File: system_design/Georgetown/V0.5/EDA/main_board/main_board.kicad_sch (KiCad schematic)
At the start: 32 parts, among them J1 B3B-XH-A_LF__SN_, J2 Conn_01x02_Pin, P1 SD card socket, SW1 SW_Wuerth_450301014042, U1 HX-2S-JH10, U2 DS3231M, U3 INA219AxD, U4 BME280_module, U5 KA78M05_TO252

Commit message: PCB updated - cosmetics
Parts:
- C1, C2, C4: value C -> 0.1uF
- C3: value C -> 22uF
- R2: value Rs -> 0.1
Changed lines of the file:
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@@
 			)
 		)
-		(property "Value" "C"
+		(property "Value" "0.1uF"
 			(at 241.3 147.5994 90)
 			(effects
@@
 			)
 		)
-		(property "Value" "Rs"
+		(property "Value" "0.1"
 			(at 98.298 43.053 0)
 			(effects
@@
 			)
 		)
-		(property "Value" "C"
+		(property "Value" "0.1uF"
 			(at 108.331 43.053 0)
 			(effects
@@
 			)
 		)
-		(property "Value" "C"
+		(property "Value" "0.1uF"
 			(at 104.521 57.023 0)
 			(effects
@@
 			)
 		)
-		(property "Value" "C"
+		(property "Value" "22uF"
 			(at 74.041 57.023 0)
 			(effects

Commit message: PCB correction for v0.5
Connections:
- net 3V3: now reaches A1.17 (3V3), C1.1, C5.1, C6.1, P1.4 (VDD), R3.1, R4.1, R5.2, U2.2 (VCC), U3.5 (VS), U4.1 (VIN), nRF24L01+1.1 (3.3V)
- net nRF_CE: now reaches A1.9 (D6)
- net nRF_CE: now also nRF24L01+1.6 (CE); no longer nRF24L01+1.2 (CSN)
- net MOSI: now reaches A1.14 (D11), R9.1, nRF24L01+1.3 (MOSI)
- net MOSI: no longer R11.1
- net at nRF24L01+1.4 (IRQ): no longer A1.6 (D3)
- net nRF_CS: now reaches A1.10 (D7)
- net nRF_CS: now also nRF24L01+1.2 (CSN); no longer nRF24L01+1.6 (CE)
- net SCK: now reaches A1.16 (D13), nRF24L01+1.7 (SCK)
- net SCK: now also R7.1
- net MISO: now reaches A1.15 (D12), P1.7 (DAT0/MISO), nRF24L01+1.8 (MISO)
- net 5V: now reaches A1.27 (+5V), C3.2, U5.3 (VO), Ultrasonic_sensor1.4 (VCC)
- net SD_CS: now reaches A1.13 (D10)
- net SD_CS: now also R11.1; no longer R7.1
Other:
- moved on the sheet: C5, C6, P1, R10, R11, R6, R7, R8, R9, nRF24L01+1

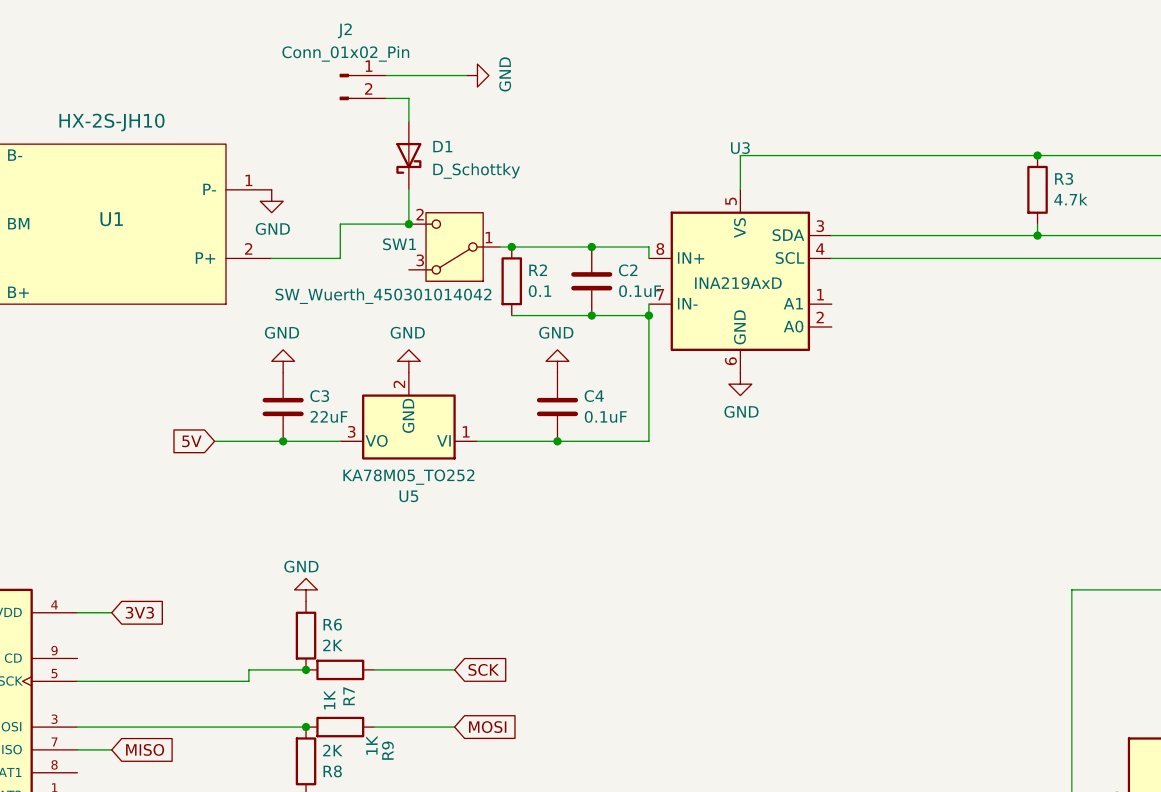
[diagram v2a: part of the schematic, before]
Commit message: PCB and chassis design changed
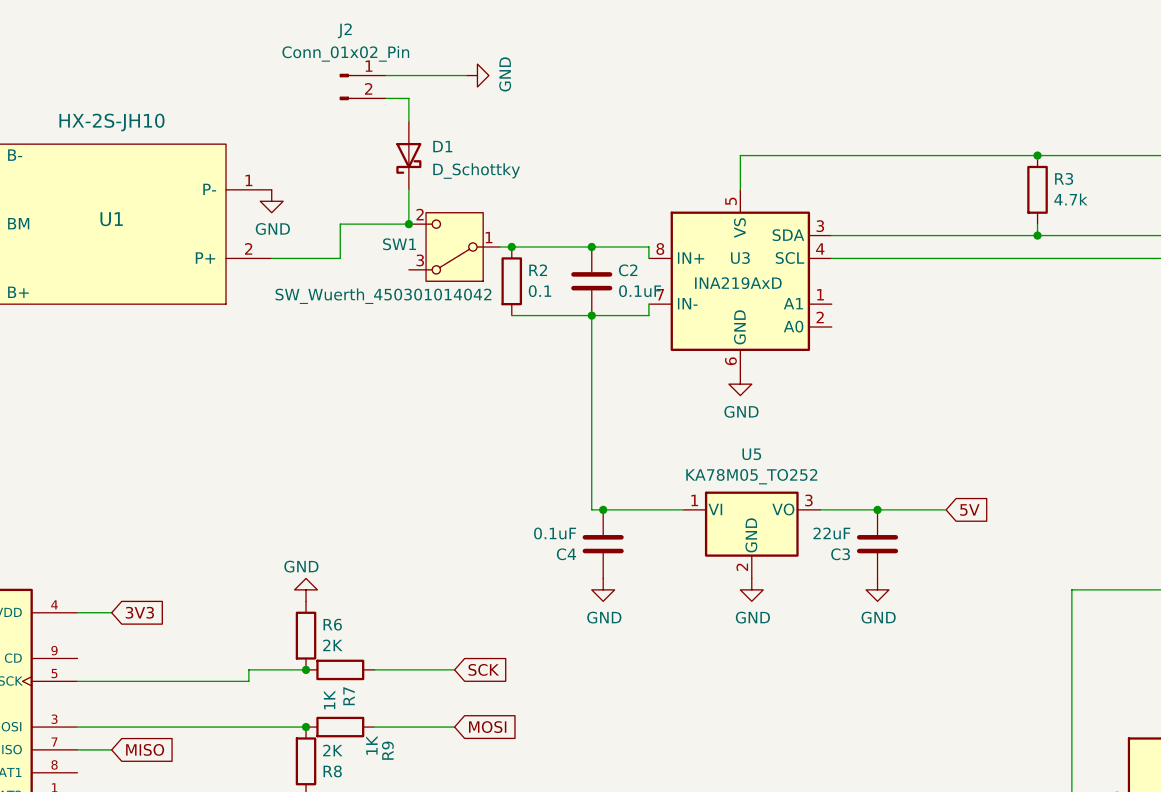
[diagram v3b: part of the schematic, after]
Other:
- moved on the sheet: C3, C4, U5
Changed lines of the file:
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@@
 	(paper "A4")
 	(junction
-		(at 111.76 45.72)
-		(diameter 0)
-		(color 0 0 0 0)
-	)
-	(junction
 		(at 204.47 119.38)
 		(diameter 0)
@@
 	)
 	(junction
-		(at 101.6 59.69)
-		(diameter 0)
-		(color 0 0 0 0)
-	)
-	(junction
 		(at 170.18 27.94)
 		(diameter 0)
@@
 	)
 	(junction
+		(at 106.68 67.31)
+		(diameter 0)
+		(color 0 0 0 0)
+	)
+	(junction
 		(at 105.41 45.72)
 		(diameter 0)
@@
 	)
 	(junction
-		(at 71.12 59.69)
+		(at 137.16 67.31)
 		(diameter 0)
 		(color 0 0 0 0)
@@
 	(wire
 		(pts
+			(xy 105.41 45.72) (xy 105.41 67.31)
+		)
+		(stroke
+			(width 0)
+			(type default)
+		)
+	)
+	(wire
+		(pts
 			(xy 52.07 153.67) (xy 54.61 153.67)
 		)
@@
 	(wire
 		(pts
-			(xy 177.8 72.39) (xy 177.8 83.82)
+			(xy 106.68 67.31) (xy 115.57 67.31)
 		)
 		(stroke
@@
 	(wire
 		(pts
-			(xy 194.31 101.6) (xy 194.31 128.27)
+			(xy 177.8 72.39) (xy 177.8 83.82)
 		)
 		(stroke
@@
 	(wire
 		(pts
-			(xy 111.76 45.72) (xy 111.76 59.69)
+			(xy 194.31 101.6) (xy 194.31 128.27)
 		)
 		(stroke
@@
 	(wire
 		(pts
+			(xy 105.41 67.31) (xy 106.68 67.31)
+		)
+		(stroke
+			(width 0)
+			(type default)
+		)
+	)
+	(wire
+		(pts
 			(xy 218.44 36.83) (xy 214.63 36.83)
 		)
@@
 	(wire
 		(pts
-			(xy 63.5 59.69) (xy 71.12 59.69)
+			(xy 144.78 67.31) (xy 137.16 67.31)
 		)
 		(stroke
@@
 	(wire
 		(pts
-			(xy 71.12 59.69) (xy 77.47 59.69)
+			(xy 137.16 67.31) (xy 130.81 67.31)
 		)
 		(stroke
@@
 	(wire
 		(pts
-			(xy 101.6 59.69) (xy 111.76 59.69)
-		)
-		(stroke
-			(width 0)
-			(type default)
-		)
-	)
-	(wire
-		(pts
 			(xy 132.08 39.37) (xy 170.18 39.37)
 		)
@@
 	(wire
 		(pts
-			(xy 92.71 59.69) (xy 101.6 59.69)
-		)
-		(stroke
-			(width 0)
-			(type default)
-		)
-	)
-	(wire
-		(pts
 			(xy 157.48 128.27) (xy 162.56 128.27)
 		)
@@
 	(global_label "5V"
 		(shape input)
-		(at 63.5 59.69 180)
+		(at 144.78 67.31 0)
 		(fields_autoplaced yes)
 		(effects
@@
 				(size 1.27 1.27)
 			)
-			(justify right)
+			(justify left)
 		)
 		(property "Intersheetrefs" "${INTERSHEET_REFS}"
-			(at 58.8709 59.69 0)
+			(at 149.4091 67.31 0)
 			(effects
 				(font
 					(size 1.27 1.27)
 				)
-				(justify right)
+				(justify left)
 				(hide yes)
 			)
@@
 	(symbol
 		(lib_id "Regulator_Linear:KA78M05_TO252")
-		(at 85.09 59.69 180)
+		(at 123.19 67.31 0)
 		(unit 1)
 		(exclude_from_sim no)
@@
 		(dnp no)
 		(property "Reference" "U5"
-			(at 85.09 65.8368 0)
+			(at 123.19 61.1632 0)
 			(effects
 				(font
@@
 		)
 		(property "Value" "KA78M05_TO252"
-			(at 85.09 63.5254 0)
+			(at 123.19 63.4746 0)
 			(effects
 				(font
@@
 		)
 		(property "Footprint" "Package_TO_SOT_SMD:SOT-223-3_TabPin2"
-			(at 85.09 65.405 0)
+			(at 123.19 61.595 0)
 			(effects
 				(font
@@
 		)
 		(property "Datasheet" "http://www.fairchildsemi.com/ds/LM/LM78M05.pdf"
-			(at 85.09 58.42 0)
+			(at 123.19 68.58 0)
 			(effects
 				(font
@@
 		)
 		(property "Description" ""
-			(at 85.09 59.69 0)
+			(at 123.19 67.31 0)
 			(effects
 				(font
@@
 		(dnp no)
 		(property "Reference" "U3"
-			(at 121.92 27.1526 0)
+			(at 121.92 39.37 0)
 			(effects
 				(font
@@
 	(symbol
 		(lib_id "main_board-rescue:GND-power")
-		(at 85.09 52.07 180)
+		(at 123.19 74.93 0)
 		(unit 1)
 		(exclude_from_sim no)
@@
 		(dnp no)
 		(property "Reference" "#PWR04"
-			(at 85.09 45.72 0)
+			(at 123.19 81.28 0)
 			(effects
 				(font
@@
 		)
 		(property "Value" "GND"
-			(at 84.963 47.6758 0)
+			(at 123.317 79.3242 0)
 			(effects
 				(font
@@
 		)
 		(property "Footprint" ""
-			(at 85.09 52.07 0)
+			(at 123.19 74.93 0)
 			(effects
 				(font
@@
 		)
 		(property "Datasheet" ""
-			(at 85.09 52.07 0)
+			(at 123.19 74.93 0)
 			(effects
 				(font
@@
 		)
 		(property "Description" ""
-			(at 85.09 52.07 0)
+			(at 123.19 74.93 0)
 			(effects
 				(font
@@
 	(symbol
 		(lib_id "Device:C")
-		(at 101.6 55.88 0)
+		(at 106.68 71.12 180)
 		(unit 1)
 		(exclude_from_sim no)
@@
 		(dnp no)
 		(property "Reference" "C4"
-			(at 104.521 54.7116 0)
+			(at 103.759 72.2884 0)
 			(effects
 				(font
@@
 		)
 		(property "Value" "0.1uF"
-			(at 104.521 57.023 0)
+			(at 103.759 69.977 0)
 			(effects
 				(font
@@
 		)
 		(property "Footprint" "Capacitor_SMD:C_1206_3216Metric_Pad1.42x1.75mm_HandSolder"
-			(at 102.5652 59.69 0)
+			(at 105.7148 67.31 0)
 			(effects
 				(font
@@
 		)
 		(property "Datasheet" "~"
-			(at 101.6 55.88 0)
+			(at 106.68 71.12 0)
 			(effects
 				(font
@@
 		)
 		(property "Description" ""
-			(at 101.6 55.88 0)
+			(at 106.68 71.12 0)
 			(effects
 				(font
@@
 	(symbol
 		(lib_id "Device:C")
-		(at 71.12 55.88 0)
+		(at 137.16 71.12 180)
 		(unit 1)
 		(exclude_from_sim no)
@@
 		(dnp no)
 		(property "Reference" "C3"
-			(at 74.041 54.7116 0)
+			(at 134.239 72.2884 0)
 			(effects
 				(font
@@
 		)
 		(property "Value" "22uF"
-			(at 74.041 57.023 0)
+			(at 134.239 69.977 0)
 			(effects
 				(font
@@
 		)
 		(property "Footprint" "Capacitor_SMD:C_1206_3216Metric_Pad1.42x1.75mm_HandSolder"
-			(at 72.0852 59.69 0)
+			(at 136.1948 67.31 0)
 			(effects
 				(font
@@
 		)
 		(property "Datasheet" "~"
-			(at 71.12 55.88 0)
+			(at 137.16 71.12 0)
 			(effects
 				(font
@@
 		)
 		(property "Description" ""
-			(at 71.12 55.88 0)
+			(at 137.16 71.12 0)
 			(effects
 				(font
@@
 	(symbol
 		(lib_id "main_board-rescue:GND-power")
-		(at 71.12 52.07 180)
+		(at 137.16 74.93 0)
 		(unit 1)
 		(exclude_from_sim no)
@@
 		(dnp no)
 		(property "Reference" "#PWR07"
-			(at 71.12 45.72 0)
+			(at 137.16 81.28 0)
 			(effects
 				(font
@@
 		)
 		(property "Value" "GND"
-			(at 70.993 47.6758 0)
+			(at 137.287 79.3242 0)
 			(effects
 				(font
@@
 		)
 		(property "Footprint" ""
-			(at 71.12 52.07 0)
+			(at 137.16 74.93 0)
 			(effects
 				(font
@@
 		)
 		(property "Datasheet" ""
-			(at 71.12 52.07 0)
+			(at 137.16 74.93 0)
 			(effects
 				(font
@@
 		)
 		(property "Description" ""
-			(at 71.12 52.07 0)
+			(at 137.16 74.93 0)
 			(effects
 				(font
@@
 	(symbol
 		(lib_id "main_board-rescue:GND-power")
-		(at 101.6 52.07 180)
+		(at 106.68 74.93 0)
 		(unit 1)
 		(exclude_from_sim no)
@@
 		(dnp no)
 		(property "Reference" "#PWR09"
-			(at 101.6 45.72 0)
+			(at 106.68 81.28 0)
 			(effects
 				(font
@@
 		)
 		(property "Value" "GND"
-			(at 101.473 47.6758 0)
+			(at 106.807 79.3242 0)
 			(effects
 				(font
@@
 		)
 		(property "Footprint" ""
-			(at 101.6 52.07 0)
+			(at 106.68 74.93 0)
 			(effects
 				(font
@@
 		)
 		(property "Datasheet" ""
-			(at 101.6 52.07 0)
+			(at 106.68 74.93 0)
 			(effects
 				(font
@@
 		)
 		(property "Description" ""
-			(at 101.6 52.07 0)
+			(at 106.68 74.93 0)
 			(effects
 				(font
